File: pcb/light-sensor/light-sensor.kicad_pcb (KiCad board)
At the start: 4 copper layers, 10.8 x 19 mm, 16 parts, among them J1 HEADER-1x04, J2 HEADER-1x01, Q1 BSS138, Q2 BSS138, U1 LP2981, U2 TSL2561

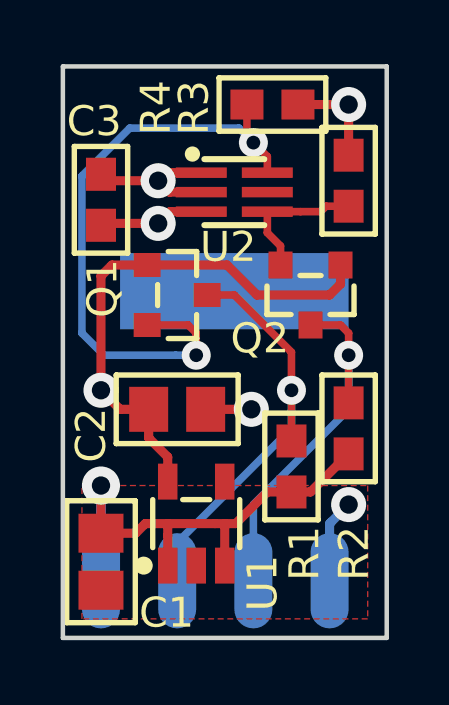
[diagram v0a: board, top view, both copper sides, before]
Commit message: Removed 3.3v regulator and level shifters
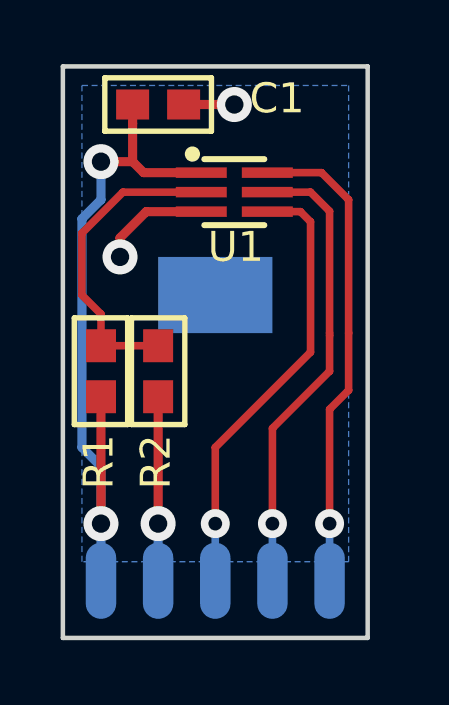
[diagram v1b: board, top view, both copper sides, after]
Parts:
- removed C2: 3.3uF, SMT:C-0805
- removed C3: 100nF, SMT:C-0603
- removed Q1, Q2: BSS138, SMT-SOT:SOT23
- removed R3, R4: 10k, SMT:R-0603
- removed U2: TSL2561, SMT-DFN:DFN6
- C1: value 1uF -> 100nF; footprint SMT:C-0805 -> SMT:C-0603
- J1: value HEADER-1x04 -> HEADER-1x05; footprint Conn-Wire-Pads:WP-50mil-1x04 -> Conn-Wire-Pads:WP-40mil-1x05
- J2: footprint Conn-Wire-Pads:SolderPad-100x300 -> Conn-Wire-Pads:SolderPad-100x150
- R1, R2: value 10k -> DNP
- U1: value LP2981 -> TSL2561; footprint SMT-SOT:SOT23-5 -> SMT-DFN:DFN6
- moved C1 15.4 mm to (107.3, 117.5), turned to 0 degrees
- moved U1 11.1 mm to (109.9, 120.4)
- moved R1 7.10 mm to (105.4, 126.4), turned to 270 degrees
- moved R2 6.63 mm to (107.3, 126.4)
- moved REF** 3.30 mm to (106.0, 121.3)
- moved J2 0.65 mm to (109.2, 123.8)
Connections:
- C1 pad 1: GND -> +3V3
- C1 pad 2: +5V -> GND
- J1 pad 1: +5V -> +3V3
- J1 pad 2: /SDA_5V -> GND
- J1 pad 3: /SCL_5V -> /SCL_3V3
- J1 pad 4: GND -> /INT
- R1 pad 1: +5V -> Net-(R1-Pad1)
- R1 pad 2: /SDA_5V -> +3V3
- R2 pad 1: +5V -> GND
- R2 pad 2: /SCL_5V -> Net-(R1-Pad1)
- U1 pad 1: +5V -> +3V3
- U1 pad 2: GND -> Net-(R1-Pad1)
- U1 pad 3: +5V -> GND
- U1 pad 4: Net-(U1-Pad4) -> /SCL_3V3
- U1 pad 5: +3V3 -> /INT
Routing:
- net +5V: track 16.9 -> 0.00 mm, vias 1 -> 0
- net /INT: track 0.00 -> 15.4 mm, vias 0 -> 1
- net /SDA_5V: track 14.5 -> 0.00 mm, vias 1 -> 0
- net /SCL_5V: track 12.5 -> 0.00 mm, vias 1 -> 0
- net Net-(R1-Pad1): track 0.00 -> 10.5 mm
- net /SCL_3V3: track 4.75 -> 14.9 mm, vias 0 -> 1
- net /SDA_3V3: track 21.0 -> 16.0 mm, vias 2 -> 1
- net GND: track 7.83 -> 11.5 mm
- net +3V3: track 26.1 -> 24.1 mm, vias 3 -> 2
- added copper zone on B.Cu, net GND
- removed copper zone on Power, net +3V3
- removed copper zone on F.Cu, net GND
- removed copper zone on GND, net GND
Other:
- board size 10.8 x 19 mm -> 10.2 x 19 mm
- copper layers 4 -> 2
- board text added: "3.3V"
- board text added: "INT"
- board text removed: "5V"

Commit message: Centered the light sensor horizontally
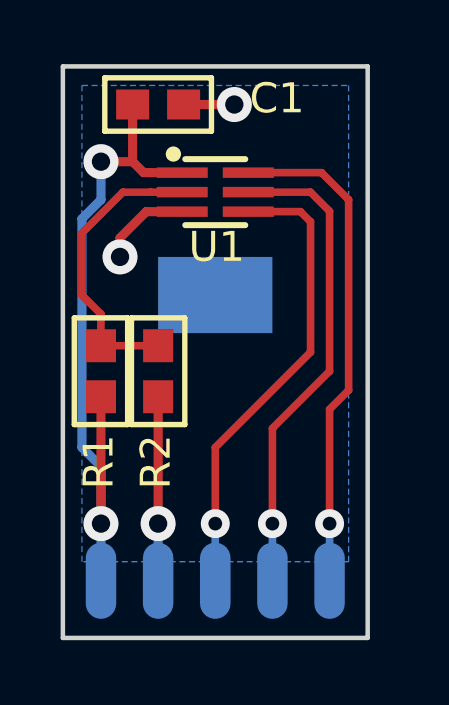
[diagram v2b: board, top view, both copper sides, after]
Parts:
- moved U1 0.64 mm to (109.2, 120.4)
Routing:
- net /INT: track 15.4 -> 16.1 mm
- net /SCL_3V3: track 14.9 -> 15.5 mm
- net /SDA_3V3: track 16.0 -> 16.7 mm
- net Net-(R1-Pad1): track 10.5 -> 9.83 mm
- net GND: track 11.5 -> 10.9 mm
- net +3V3: track 24.1 -> 23.5 mm
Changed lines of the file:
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@@
     (thickness 1.6)
     (drawings 23)
-    (tracks 53)
+    (tracks 52)
     (zones 0)
     (modules 9)
@@
   (title_block
     (title "Ambient light sensor")
-    (date 2016-07-15)
+    (date 2016-07-22)
     (rev A)
     (comment 1 CLKV3-PC-07)
@@
   )
   (module SMT-DFN:DFN6 (layer F.Cu)
-    (at 109.855 120.396)
+    (at 109.22 120.396)
     (descr "DFN - 6")
     (fp_text reference U1 (at -0.889 2.413) (layer F.SilkS)
@@
   (gr_line (start 114.3 135.255) (end 114.3 116.205) (layer Edge.Cuts) (width 0.15))
   (gr_line (start 104.14 135.255) (end 114.3 135.255) (layer Edge.Cuts) (width 0.15))
-  (segment (start 108.755 121.046) (end 106.919 121.046) (width 0.3048) (layer F.Cu) (net 1))
+  (segment (start 106.919 121.046) (end 108.12 121.046) (width 0.3048) (layer F.Cu) (net 1))
   (segment (start 106.919 121.046) (end 106.045 121.92) (width 0.3048) (layer F.Cu) (net 1))
   (segment (start 106.045 121.92) (end 106.045 122.555) (width 0.3048) (layer F.Cu) (net 1))
@@
   (segment (start 107.315 127.215) (end 107.315 131.445) (width 0.3048) (layer F.Cu) (net 1))
   (via (at 107.315 131.445) (size 1.1684) (drill 0.6096) (layers F.Cu B.Cu) (net 1))
+  (segment (start 106.831 119.746) (end 107.046 119.746) (width 0.3048) (layer F.Cu) (net 3))
+  (segment (start 107.046 119.746) (end 108.12 119.746) (width 0.3048) (layer F.Cu) (net 3))
   (segment (start 106.465 118.11) (end 106.465 117.475) (width 0.3048) (layer F.Cu) (net 3))
   (segment (start 105.41 131.445) (end 105.41 129.54) (width 0.3048) (layer B.Cu) (net 3))
@@
   (segment (start 105.41 131.445) (end 105.41 133.35) (width 0.3048) (layer B.Cu) (net 3))
   (segment (start 106.465 119.38) (end 106.831 119.746) (width 0.3048) (layer F.Cu) (net 3))
-  (segment (start 106.831 119.746) (end 108.755 119.746) (width 0.3048) (layer F.Cu) (net 3))
   (segment (start 105.41 119.38) (end 106.465 119.38) (width 0.3048) (layer F.Cu) (net 3))
   (segment (start 106.465 118.11) (end 106.465 119.38) (width 0.3048) (layer F.Cu) (net 3))
@@
   (segment (start 105.41 127.215) (end 105.41 131.445) (width 0.3048) (layer F.Cu) (net 3))
   (via (at 105.41 131.445) (size 1.1684) (drill 0.6096) (layers F.Cu B.Cu) (net 3))
+  (segment (start 110.32 119.746) (end 112.761 119.746) (width 0.254) (layer F.Cu) (net 4))
+  (segment (start 112.761 119.746) (end 113.665 120.65) (width 0.254) (layer F.Cu) (net 4))
+  (segment (start 113.03 127.635) (end 113.03 131.445) (width 0.254) (layer F.Cu) (net 4))
+  (segment (start 113.665 120.65) (end 113.665 127) (width 0.254) (layer F.Cu) (net 4))
+  (segment (start 113.665 127) (end 113.03 127.635) (width 0.254) (layer F.Cu) (net 4))
   (segment (start 113.03 131.445) (end 113.03 133.35) (width 0.254) (layer B.Cu) (net 4))
-  (segment (start 113.665 127) (end 113.03 127.635) (width 0.254) (layer F.Cu) (net 4))
-  (segment (start 113.03 127.635) (end 113.03 131.445) (width 0.254) (layer F.Cu) (net 4))
   (via (at 113.03 131.445) (size 0.9652) (drill 0.4572) (layers F.Cu B.Cu) (net 4))
-  (segment (start 113.665 125.095) (end 113.665 127) (width 0.254) (layer F.Cu) (net 4))
-  (segment (start 110.955 119.746) (end 112.761 119.746) (width 0.254) (layer F.Cu) (net 4))
-  (segment (start 112.761 119.746) (end 113.665 120.65) (width 0.254) (layer F.Cu) (net 4))
-  (segment (start 113.665 120.65) (end 113.665 125.095) (width 0.254) (layer F.Cu) (net 4))
-  (segment (start 110.955 121.046) (end 112.059 121.046) (width 0.254) (layer F.Cu) (net 5))
+  (segment (start 110.32 121.046) (end 112.059 121.046) (width 0.254) (layer F.Cu) (net 5))
   (segment (start 112.059 121.046) (end 112.395 121.382) (width 0.254) (layer F.Cu) (net 5))
   (segment (start 112.395 125.73) (end 109.22 128.905) (width 0.254) (layer F.Cu) (net 5))
@@
   (segment (start 109.22 131.445) (end 109.22 133.35) (width 0.254) (layer B.Cu) (net 5))
   (via (at 109.22 131.445) (size 0.9652) (drill 0.4572) (layers F.Cu B.Cu) (net 5))
-  (segment (start 111.125 131.445) (end 111.125 133.35) (width 0.254) (layer B.Cu) (net 6))
+  (segment (start 110.32 120.396) (end 112.395 120.396) (width 0.254) (layer F.Cu) (net 6))
+  (segment (start 112.395 120.396) (end 113.03 121.031) (width 0.254) (layer F.Cu) (net 6))
+  (segment (start 113.03 121.031) (end 113.03 126.365) (width 0.254) (layer F.Cu) (net 6))
   (segment (start 113.03 126.365) (end 111.125 128.27) (width 0.254) (layer F.Cu) (net 6))
   (segment (start 111.125 128.27) (end 111.125 131.445) (width 0.254) (layer F.Cu) (net 6))
+  (segment (start 111.125 131.445) (end 111.125 133.35) (width 0.254) (layer B.Cu) (net 6))
   (via (at 111.125 131.445) (size 0.9652) (drill 0.4572) (layers F.Cu B.Cu) (net 6))
-  (segment (start 113.03 125.178434) (end 113.03 126.365) (width 0.254) (layer F.Cu) (net 6))
-  (segment (start 113.03 125.095) (end 113.03 125.178434) (width 0.254) (layer F.Cu) (net 6))
-  (segment (start 110.955 120.396) (end 112.395 120.396) (width 0.254) (layer F.Cu) (net 6))
-  (segment (start 112.395 120.396) (end 113.03 121.031) (width 0.254) (layer F.Cu) (net 6))
-  (segment (start 113.03 121.031) (end 113.03 125.095) (width 0.254) (layer F.Cu) (net 6))
-  (segment (start 108.755 120.396) (end 106.1405 120.396) (width 0.254) (layer F.Cu) (net 7))
+  (segment (start 106.1405 120.396) (end 107.061 120.396) (width 0.254) (layer F.Cu) (net 7))
+  (segment (start 107.061 120.396) (end 108.12 120.396) (width 0.254) (layer F.Cu) (net 7))
   (segment (start 106.1405 120.396) (end 104.775 121.7615) (width 0.254) (layer F.Cu) (net 7))
   (segment (start 104.775 121.7615) (end 104.775 123.825) (width 0.254) (layer F.Cu) (net 7))
